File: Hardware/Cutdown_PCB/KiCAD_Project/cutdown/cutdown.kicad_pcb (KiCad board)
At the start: 4 copper layers, 24.1 x 60.3 mm, 26 parts, among them J1 Nichrome Wire, Q1 MMBT3904, U1 Particle, U2 BMP388, U3 ublox_SAM-M8Q

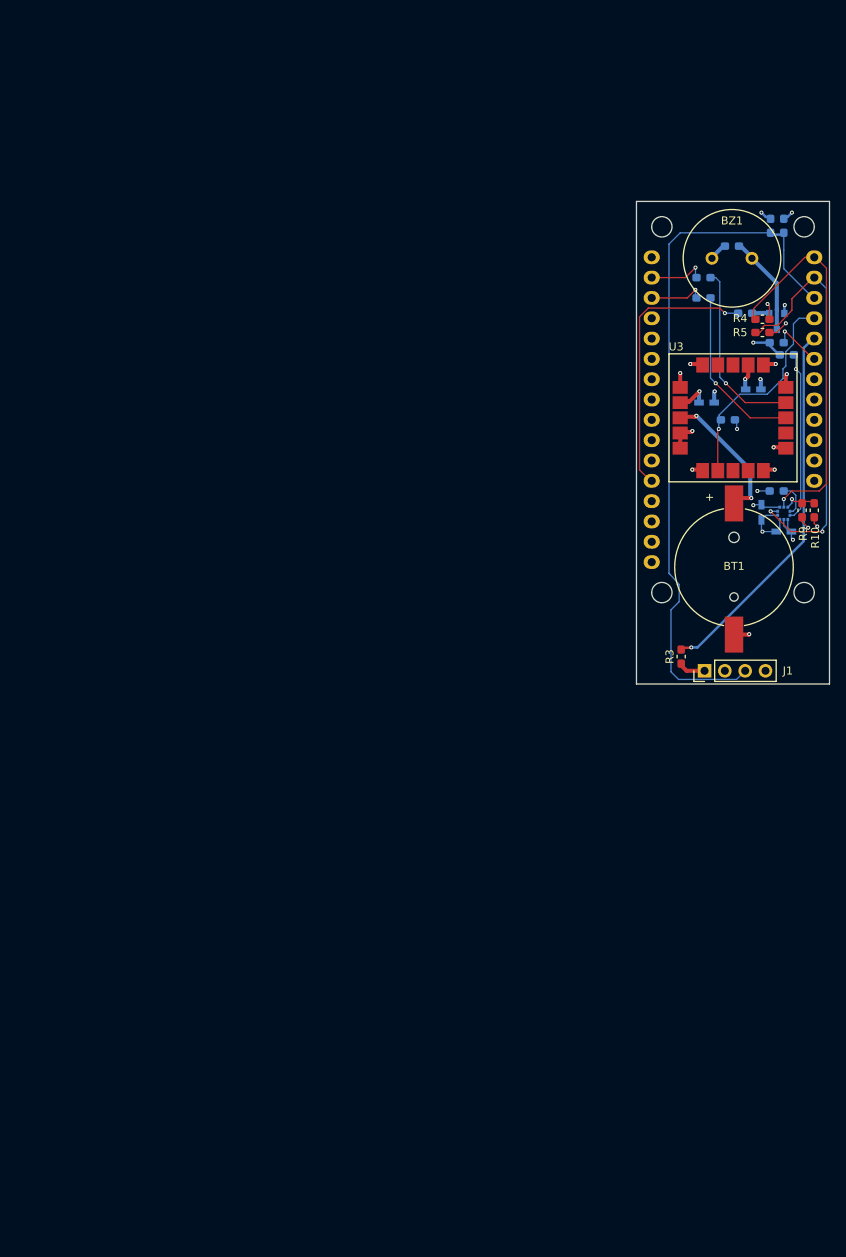
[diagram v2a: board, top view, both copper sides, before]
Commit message: Remove cutdown power pcb and update cutdown design
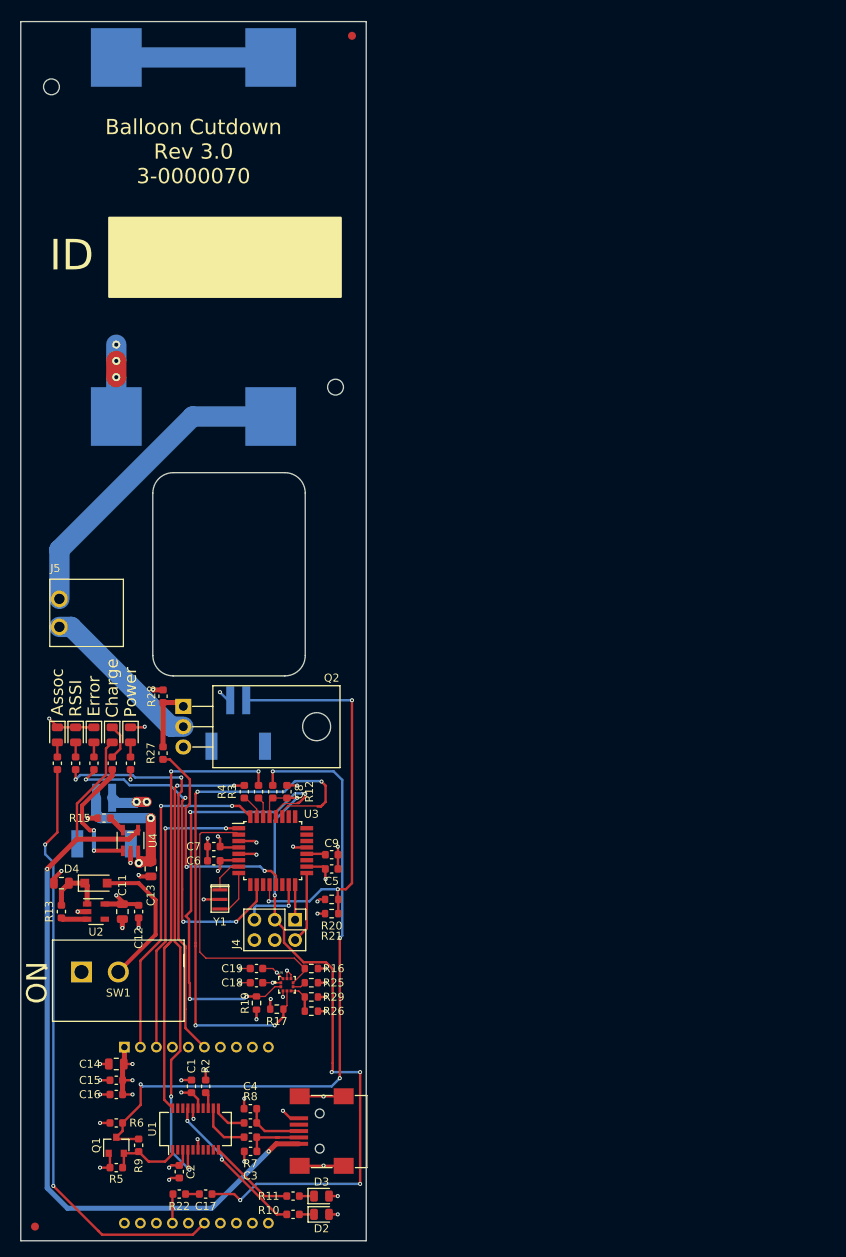
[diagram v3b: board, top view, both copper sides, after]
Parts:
- removed BZ1: Buzzer, lib_fp:PS1240P02BT
- added BT2: CR123, lib_fp:1-0000782, B.Cu at (133.3, 52.1)
- added C10: 1-0000075, capacitors_0805:1-0000075, F.Cu at (107.2, 132.8)
- added C11: 1-0000075, capacitors_0805:1-0000075, F.Cu at (114.8, 136.4)
- added C12: 1-0000018, capacitors_0603:1-0000018, F.Cu at (116.8, 136.4)
- added C13: 1-0000075, capacitors_0805:1-0000075, F.Cu at (118.4, 131.1)
- added C14: 1-0000075, capacitors_0805:1-0000075, F.Cu at (114.0, 155.4)
- added C15: 1-0000018, capacitors_0603:1-0000018, F.Cu at (114.0, 157.5)
- added C16: 1-0000007, capacitors_0603:1-0000007, F.Cu at (114.0, 159.3)
- added C17: 1-0000007, capacitors_0603:1-0000007, F.Cu at (125.2, 171.7)
- added C18: 0.1u, Capacitor_SMD:C_0603_1608Metric, F.Cu at (131.6, 145.3)
- added C19: 0.1u, Capacitor_SMD:C_0603_1608Metric, F.Cu at (131.6, 143.5)
- added C5: 1-0000007, capacitors_0603:1-0000007, F.Cu at (141.0, 131.1)
- added C6: 1-0000007, capacitors_0603:1-0000007, F.Cu at (126.2, 130.0)
- added C7: 1-0000007, capacitors_0603:1-0000007, F.Cu at (126.2, 128.3)
- added C8: 1-0000007, capacitors_0603:1-0000007, F.Cu at (133.6, 121.4)
- added C9: 1-0000007, capacitors_0603:1-0000007, F.Cu at (141.0, 129.3)
- added D1: Green, LED_SMD:LED_0805_2012Metric, F.Cu at (115.8, 114.3)
- added D2: Yellow, LED_SMD:LED_0805_2012Metric, F.Cu at (139.7, 174.2)
- added D3: Red, LED_SMD:LED_0805_2012Metric, F.Cu at (139.7, 172.0)
- added D4: D_Schottky, Diode_SMD:D_SOD-123F, F.Cu at (111.5, 132.8)
- added D5: Yellow, LED_SMD:LED_0805_2012Metric, F.Cu at (113.5, 114.3)
- added D6: Red, LED_SMD:LED_0805_2012Metric, F.Cu at (111.3, 114.3)
- added D7: Blue, LED_SMD:LED_0805_2012Metric, F.Cu at (109.0, 114.3)
- added D8: Yellow, LED_SMD:LED_0805_2012Metric, F.Cu at (106.7, 114.3)
- added FID1: Fiducial, Fiducial:Fiducial_1mm_Mask2mm, F.Cu at (143.5, 26.9)
- added FID2: Fiducial, Fiducial:Fiducial_1mm_Mask2mm, F.Cu at (103.9, 175.8)
- added J2: Battery LiPO 1S, lib_fp:JST_S2B-PH-SM4-TB(LF)(SN), B.Cu at (112.5, 122.2)
- added J3: External Cutdown, lib_fp:JST_S2B-PH-SM4-TB(LF)(SN), B.Cu at (129.3, 110.0)
- added J4: ISP, Connector_PinHeader_2.54mm:PinHeader_2x03_P2.54mm_Vertical, F.Cu at (136.4, 137.4)
- added J5: Hot Wire, lib_fp:1-0000783, F.Cu at (106.9, 99.1)
- added PCB1: barepcb, lib_fp:barepcb, F.Cu at (278.6, 161.5)
- added Q2: FQP30N06L, Package_TO_SOT_THT:TO-220-3_Horizontal_TabDown, F.Cu at (122.4, 110.7)
- added R16: 10k, Resistor_SMD:R_0603_1608Metric, F.Cu at (138.4, 143.5)
- added R17: 10k, Resistor_SMD:R_0603_1608Metric, F.Cu at (134.1, 148.6)
- added R18: 1-0000008, resistors_0603:1-0000008, F.Cu at (111.3, 117.9)
- added R19: 10k, Resistor_SMD:R_0603_1608Metric, F.Cu at (131.6, 147.8)
- added R20: 10k, Resistor_SMD:R_0603_1608Metric, F.Cu at (141.0, 134.9)
- added R21: NP, Resistor_SMD:R_0603_1608Metric, F.Cu at (141.0, 136.7)
- added R22: 1-0000006, resistors_0603:1-0000006, F.Cu at (121.9, 171.7)
- added R23: 1-0000008, resistors_0603:1-0000008, F.Cu at (109.0, 117.9)
- added R24: 1-0000008, resistors_0603:1-0000008, F.Cu at (106.7, 117.9)
- added R25: 10k, Resistor_SMD:R_0603_1608Metric, F.Cu at (138.4, 145.3)
- added R26: NP, Resistor_SMD:R_0603_1608Metric, F.Cu at (138.4, 148.8)
- added R27: 1-0000006, resistors_0603:1-0000006, F.Cu at (119.9, 116.6)
- added R28: 1-0000010, resistors_0603:1-0000010, F.Cu at (119.9, 109.5)
- added R29: 10k, Resistor_SMD:R_0603_1608Metric, F.Cu at (138.4, 147.1)
- added SW1: SW_SPST, lib_fp:SW_GF-123-0054, F.Cu at (114.3, 145.0)
- added U4: MCP73831, lib_fp:1-0000793, F.Cu at (115.8, 127.5)
- added U5: XBee, lib_fp:XBee, B.Cu at (115.1, 164.3)
- added U6: BMP388, lib_fp:PQFN50P200X200X80-10N, F.Cu at (135.4, 145.5)
- added Y1: 16MHz, lib_fp:Resonator, F.Cu at (127.0, 134.9)
- BT1: value CR1220 -> CR123; footprint lib_fp:S8411-45R -> lib_fp:1-0000782; moved to B.Cu
- C1, C2: value 0.1u -> 1-0000007; footprint Capacitors_SMD:C_0603_HandSoldering -> capacitors_0603:1-0000007; moved to F.Cu
- C3, C4: value 0.1u -> 1-0000017; footprint Capacitors_SMD:C_0603_HandSoldering -> capacitors_0603:1-0000017; moved to F.Cu
- J1: value Nichrome Wire -> Mini_USB_B; footprint Pin_Headers:Pin_Header_Straight_1x04_Pitch2.54mm -> lib_fp:MiniUSB
- Q1: value MMBT3904 -> 2N7002; footprint TO_SOT_Packages_SMD:SOT-23 -> Package_TO_SOT_SMD:SOT-23; moved to F.Cu
- R1: value 10k -> 1-0000008; footprint Resistor_SMD:R_0603_1608Metric_Pad1.05x0.95mm_HandSolder -> resistors_0603:1-0000008; moved to F.Cu
- R10: value 10k -> 1-0000008; footprint Resistor_SMD:R_0603_1608Metric_Pad1.05x0.95mm_HandSolder -> resistors_0603:1-0000008
- R11: value 1k -> 1-0000008; footprint Resistor_SMD:R_0603_1608Metric_Pad1.05x0.95mm_HandSolder -> resistors_0603:1-0000008; moved to F.Cu
- R12: value 1k -> 1-0000010; footprint Resistor_SMD:R_0603_1608Metric_Pad1.05x0.95mm_HandSolder -> resistors_0603:1-0000010; moved to F.Cu
- R13: value 10k -> 1-0000174; footprint Resistor_SMD:R_0603_1608Metric_Pad1.05x0.95mm_HandSolder -> resistors_0603:1-0000174; moved to F.Cu
- R14: value 0R0 -> 1-0000013; footprint Resistor_SMD:R_0603_1608Metric_Pad1.05x0.95mm_HandSolder -> resistors_0603:1-0000013; moved to F.Cu
- R15: value 0R0 -> 1-0000010; footprint Resistor_SMD:R_0603_1608Metric_Pad1.05x0.95mm_HandSolder -> resistors_0603:1-0000010; moved to F.Cu
- R2: value 10k -> 1-0000006; footprint Resistor_SMD:R_0603_1608Metric_Pad1.05x0.95mm_HandSolder -> resistors_0603:1-0000006; moved to F.Cu
- R3: value 0R0 -> 1-0000013; footprint Resistor_SMD:R_0603_1608Metric_Pad1.05x0.95mm_HandSolder -> resistors_0603:1-0000013
- R4: value 10k -> 1-0000013; footprint Resistor_SMD:R_0603_1608Metric_Pad1.05x0.95mm_HandSolder -> resistors_0603:1-0000013
- R5: value 10k -> 1-0000010; footprint Resistor_SMD:R_0603_1608Metric_Pad1.05x0.95mm_HandSolder -> resistors_0603:1-0000010
- R6: value 10k -> 1-0000010; footprint Resistor_SMD:R_0603_1608Metric_Pad1.05x0.95mm_HandSolder -> resistors_0603:1-0000010; moved to F.Cu
- R7: value 10k -> 1-0000012; footprint Resistor_SMD:R_0603_1608Metric_Pad1.05x0.95mm_HandSolder -> resistors_0603:1-0000012; moved to F.Cu
- R8: value NP -> 1-0000012; footprint Resistor_SMD:R_0603_1608Metric_Pad1.05x0.95mm_HandSolder -> resistors_0603:1-0000012; moved to F.Cu
- R9: value NP -> 1-0000006; footprint Resistor_SMD:R_0603_1608Metric_Pad1.05x0.95mm_HandSolder -> resistors_0603:1-0000006
- U1: value Particle -> FT231XS; footprint lib_fp:Particle -> Package_SO:SSOP-20_3.9x8.7mm_P0.635mm; moved to F.Cu
- U2: value BMP388 -> SPX3819M5-L-3-3; footprint lib_fp:PQFN50P200X200X80-10N -> Package_TO_SOT_SMD:SOT-23-5; moved to F.Cu
- U3: value ublox_SAM-M8Q -> ATmega328P-AU; footprint lib_fp:SAM-M8Q -> Package_QFP:TQFP-32_7x7mm_P0.8mm
- moved R7 132.0 mm to (130.8, 164.6), turned to 0 degrees
- moved R5 132.0 mm to (114.0, 168.4)
- moved Q1 132.0 mm to (114.0, 165.6), turned to 90 degrees
- moved R8 129.6 mm to (130.8, 162.8), turned to 0 degrees
- moved R11 124.0 mm to (136.1, 172.0)
- moved R2 116.8 mm to (125.2, 158.2), turned to 90 degrees
- moved R6 116.5 mm to (114.0, 162.8)
- moved R9 114.8 mm to (116.8, 165.6)
- moved C3 114.1 mm to (130.8, 166.4)
- moved U1 112.2 mm to (124.0, 163.6)
- moved C2 110.1 mm to (121.9, 168.9), turned to 270 degrees
- moved R10 109.5 mm to (136.1, 174.2), turned to 180 degrees
- moved C4 105.1 mm to (130.8, 161.0)
- moved R13 103.7 mm to (107.2, 136.4), turned to 270 degrees
- moved C1 101.1 mm to (123.4, 158.2)
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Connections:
- BT1 pad 1: +BATT -> Net-(BT1-Pad1)
- C2 pad 1: GND -> +3V3
- C2 pad 2: +3V3 -> GND
- C3 pad 1: GND -> Net-(C3-Pad1)
- C3 pad 2: +3V3 -> GND
- C4 pad 1: GND -> Net-(C4-Pad1)
- C4 pad 2: +3V3 -> GND
- J1 pad 1: Net-(J1-Pad1) -> +5V
- J1 pad 2: GND -> Net-(C3-Pad1)
- J1 pad 3: EXT_CUTDOWN -> Net-(C4-Pad1)
- J1 pad 4: GND -> (no net)
- Q1 pad 1: Net-(Q1-Pad1) -> +3V3
- Q1 pad 2: GND -> Net-(Q1-Pad2)
- Q1 pad 3: Net-(BZ1-Pad2) -> DTR
- R1 pad 1: +3V3 -> Net-(D1-Pad2)
- R1 pad 2: BMP388_SDO -> +3V3
- R10 pad 1: Net-(R10-Pad1) -> Net-(D2-Pad1)
- R10 pad 2: GND -> Net-(R10-Pad2)
- R11 pad 1: Net-(Q1-Pad1) -> Net-(D3-Pad1)
- R11 pad 2: PIEZO_ELEMENT -> Net-(R11-Pad2)
- R12 pad 2: Net-(BZ1-Pad2) -> RESET
- R13 pad 1: +3V3 -> Net-(C10-Pad1)
- R14 pad 2: GPS_TX -> Net-(D5-Pad1)
- R15 pad 2: GPS_RX -> GND
- R2 pad 1: +3V3 -> Net-(R2-Pad1)
- R2 pad 2: BMP388_INT -> +3V3
- R3 pad 1: Net-(J1-Pad1) -> RXI
- R3 pad 2: CUTOFF_LOGIC -> Net-(R3-Pad2)
- R4 pad 1: +3V3 -> TXO
- R4 pad 2: SDA -> Net-(R4-Pad2)
- R5 pad 1: +3V3 -> Net-(Q1-Pad2)
- R5 pad 2: SCL -> +3V3
- R6 pad 1: +3V3 -> DTR
- R6 pad 2: GPS_PPS -> +3V3
- R7 pad 1: +3V3 -> Net-(R7-Pad1)
- R7 pad 2: EXT_CUTDOWN -> Net-(C3-Pad1)
- R8 pad 1: GND -> Net-(R8-Pad1)
- R8 pad 2: EXT_CUTDOWN -> Net-(C4-Pad1)
- R9 pad 1: +3V3 -> Net-(Q1-Pad2)
- R9 pad 2: Net-(R10-Pad1) -> DTR
- U1 pad 1: Net-(U1-Pad1) -> Net-(Q1-Pad2)
- U1 pad 10: Net-(U1-Pad10) -> Net-(R11-Pad2)
- U1 pad 11: Net-(U1-Pad11) -> Net-(R8-Pad1)
- U1 pad 12: Net-(U1-Pad12) -> Net-(R7-Pad1)
- U1 pad 13: Net-(U1-Pad13) -> Net-(R2-Pad1)
- U1 pad 14: Net-(R14-Pad1) -> (no net)
- U1 pad 15: Net-(R15-Pad1) -> +3V3
- U1 pad 16: Net-(U1-Pad16) -> GND
- U1 pad 17: Net-(U1-Pad17) -> Net-(R10-Pad2)
- U1 pad 18: Net-(U1-Pad18) -> (no net)
- U1 pad 19: Net-(U1-Pad19) -> (no net)
- U1 pad 2: +3V3 -> (no net)
- U1 pad 20: Net-(U1-Pad20) -> Net-(R3-Pad2)
- U1 pad 3: Net-(U1-Pad3) -> +3V3
- U1 pad 4: GND -> Net-(R4-Pad2)
- U1 pad 5: PIEZO_ELEMENT -> (no net)
- U1 pad 6: Net-(U1-Pad6) -> GND
- U1 pad 7: Net-(U1-Pad7) -> (no net)
- U1 pad 8: Net-(U1-Pad8) -> (no net)
- U1 pad 9: Net-(U1-Pad9) -> (no net)
- U2 pad 1: +3V3 -> Net-(C10-Pad1)
- U2 pad 2: SCL -> GND
- U2 pad 3: GND -> Net-(R13-Pad2)
- U2 pad 4: SDA -> (no net)
- U2 pad 5: Net-(R10-Pad1) -> +3V3
- U3 pad 1: GND -> XBee_from_uC
- U3 pad 10: GND -> Net-(R18-Pad2)
- U3 pad 11: GND -> (no net)
- U3 pad 12: Net-(U3-Pad12) -> EXT_CUTDOWN
- U3 pad 13: GPS_TX -> Cutdown_Command
- U3 pad 14: GPS_RX -> (no net)
- U3 pad 15: GND -> MOSI
- U3 pad 16: GND -> MISO
- U3 pad 17: +3V3 -> SCK
- U3 pad 18: Net-(U3-Pad18) -> +3V3
- U3 pad 19: Net-(U3-Pad19) -> (no net)
- U3 pad 2: +3V3 -> BMP388_INT
- U3 pad 20: GND -> Net-(C9-Pad1)
- U3 pad 3: +BATT -> GND
- U3 pad 4: GND -> +3V3
- U3 pad 6: GND -> +3V3
- U3 pad 7: GPS_PPS -> Net-(U3-Pad7)
- U3 pad 9: Net-(U3-Pad9) -> (no net)
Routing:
- net +5V: track 0.00 -> 103.0 mm, vias 0 -> 2
- net DTR: track 0.00 -> 84.5 mm, vias 0 -> 4
- net RESET: track 0.00 -> 82.9 mm, vias 0 -> 6
- net Net-(R24-Pad2): track 0.00 -> 75.1 mm, vias 0 -> 2
- net Net-(R4-Pad2): track 0.00 -> 60.8 mm, vias 0 -> 4
- net Net-(R3-Pad2): track 0.00 -> 56.4 mm, vias 0 -> 2
- net GND: track 30.3 -> 80.7 mm, vias 16 -> 40
- net Net-(R23-Pad1): track 0.00 -> 50.0 mm, vias 0 -> 2
- net CUTOFF_LOGIC: track 46.8 -> 0.00 mm, vias 1 -> 0
- net Net-(R18-Pad2): track 0.00 -> 43.6 mm, vias 0 -> 4
- net XBee_to_uC: track 0.00 -> 42.9 mm, vias 0 -> 2
- net Net-(BT2-Pad1): track 0.00 -> 39.5 mm
- net XBee_from_uC: track 0.00 -> 37.0 mm, vias 0 -> 2
- net EXT_CUTDOWN: track 89.0 -> 52.6 mm, vias 0 -> 3
- net PIEZO_ELEMENT: track 34.0 -> 0.00 mm, vias 1 -> 0
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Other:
- board size 24.1 x 60.3 mm -> 43.2 x 152.4 mm
- board text added: "Assoc"
- board text added: "BATT"
- board text added: "Balloon Cutdown Rev 3.0 3-0000070"
- board text added: "Charge"
- board text added: "EXT"
- board text added: "Error"
- board text added: "ID"
- board text added: "ON"
- board text added: "Power"
- board text added: "RSSI"
- board text removed: "Balloon Cutdown Module Rev. 2.0 April 2020 P/N 3-0000028"
- board text removed: "Cut"
- board text removed: "Ext"

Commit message: Tweaks
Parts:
- moved J5 5.07 mm to (105.0, 94.4)
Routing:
- net Net-(J5-Pad2): track 20.7 -> 32.3 mm
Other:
- outline, holes or cut-outs redrawn
- board text added: "Chg"
- board text added: "Err"
- board text added: "Pwr"
- board text removed: "Charge"
- board text removed: "Error"
- board text removed: "Power"

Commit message: Update production files
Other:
- rule pad_to_mask_clearance: 0.0508 -> 0

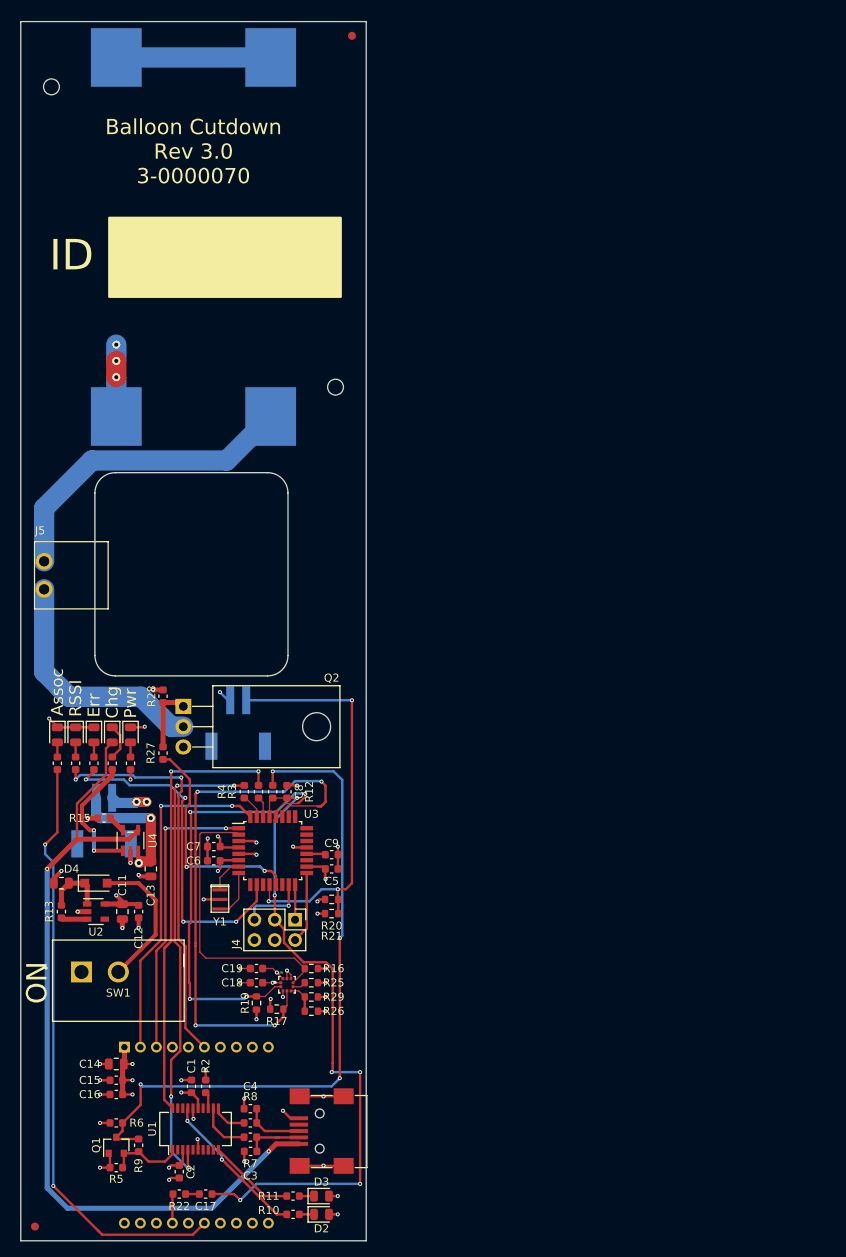
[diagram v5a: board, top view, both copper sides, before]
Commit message: Move batteries, remove charging circuit, add mounting holes.
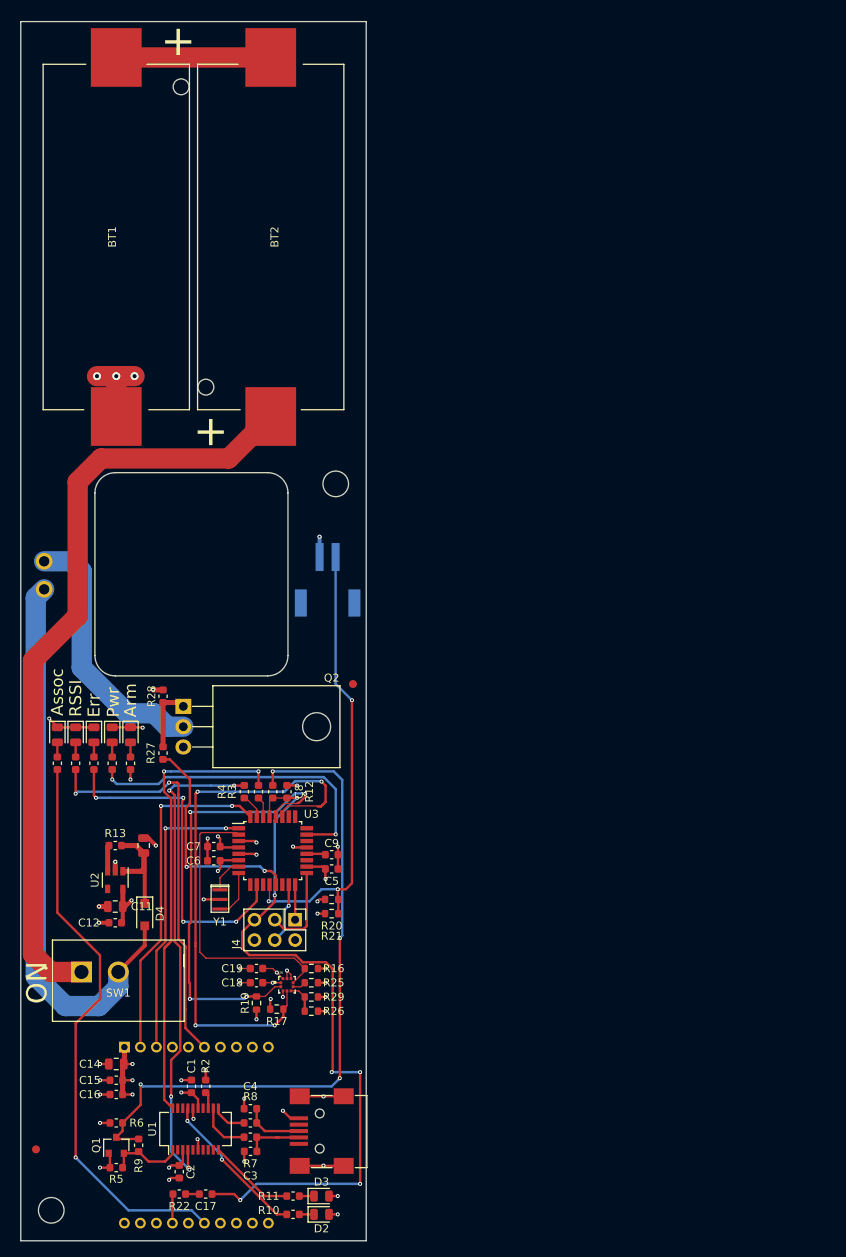
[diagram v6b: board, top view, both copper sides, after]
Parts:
- removed C13: 1-0000075, capacitors_0805:1-0000075
- removed J2: Battery LiPO 1S, lib_fp:JST_S2B-PH-SM4-TB(LF)(SN)
- removed R15: 1-0000010, resistors_0603:1-0000010
- removed U4: MCP73831, lib_fp:1-0000793
- added H1: M3_ISO_7380, mechanical:MountingHole_3.2mm_M3_ISO7380, F.Cu at (105.9, 173.7)
- added H2: M3_ISO_7380, mechanical:MountingHole_3.2mm_M3_ISO7380, F.Cu at (141.5, 82.9)
- BT1, BT2: moved to F.Cu
- D5: value Yellow -> 1-0000601; footprint LED_SMD:LED_0805_2012Metric -> leds_0805:1-0000601
- J5: moved to B.Cu
- R14: value 1-0000013 -> 1-0000008; footprint resistors_0603:1-0000013 -> resistors_0603:1-0000008
- Y1: value 16MHz -> 8MHz
- moved FID1 81.0 mm to (143.6, 108.0)
- moved J3 21.1 mm to (140.5, 92.1)
- moved C10 11.3 mm to (117.5, 128.1), turned to 90 degrees
- moved R13 10.7 mm to (113.9, 128.1), turned to 180 degrees
- moved FID2 9.65 mm to (104.0, 166.1)
- moved D4 7.26 mm to (117.6, 136.8), turned to 270 degrees
- moved U2 4.62 mm to (113.9, 132.5), turned to 270 degrees
- moved C12 3.24 mm to (113.9, 137.8), turned to 180 degrees
- moved C11 1.09 mm to (113.9, 135.8), turned to 180 degrees
- turned J5 to 90 degrees
- turned R14 to 270 degrees
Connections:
- C10 pad 1: Net-(C10-Pad1) -> +BATT
- D4 pad 1: Net-(C10-Pad1) -> +BATT
- D4 pad 2: Net-(D4-Pad2) -> SW_PWR
- D5 pad 1: Net-(D5-Pad1) -> GND
- D5 pad 2: +5V -> Net-(D5-Pad2)
- J1 pad 1: +5V -> (no net)
- J4 pad 2: SCK -> +3V3
- J4 pad 3: RESET -> SCK
- J4 pad 4: GND -> MOSI
- J4 pad 5: MOSI -> RESET
- J4 pad 6: +3V3 -> GND
- J5 pad 1: Net-(BT2-Pad1) -> SW_PWR
- R13 pad 1: Net-(C10-Pad1) -> +BATT
- R14 pad 1: Net-(R14-Pad1) -> Net-(D5-Pad2)
- R14 pad 2: Net-(D5-Pad1) -> Net-(R14-Pad2)
- SW1 pad 1: +BATT -> Net-(BT2-Pad1)
- SW1 pad 2: Net-(D4-Pad2) -> SW_PWR
- U2 pad 1: Net-(C10-Pad1) -> +BATT
- U3 pad 23: (no net) -> Net-(R14-Pad2)
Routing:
- net +5V: track 103.0 -> 0.00 mm, vias 2 -> 0
- net SW_PWR: track 0.00 -> 70.7 mm
- net Net-(BT2-Pad1): track 39.7 -> 103.0 mm
- net Net-(R14-Pad2): track 0.00 -> 39.7 mm, vias 0 -> 2
- net +BATT: track 35.6 -> 14.2 mm, vias 2 -> 0
- net Net-(D4-Pad2): track 17.9 -> 0.00 mm
- net Net-(R14-Pad1): track 16.2 -> 0.00 mm, vias 2 -> 0
- net Net-(C10-Pad1): track 7.87 -> 0.00 mm
- net RESET: track 82.9 -> 89.9 mm
- net EXT_CUTDOWN: track 52.6 -> 58.2 mm
- net GND: track 80.7 -> 75.3 mm, vias 40 -> 35
- net Net-(D5-Pad1): track 4.54 -> 0.00 mm
- net Net-(R24-Pad2): track 75.1 -> 71.5 mm, vias 2 -> 1
- net SCK: track 8.98 -> 11.3 mm
- net Net-(R15-Pad1): track 2.19 -> 0.00 mm
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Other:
- board text added: "Arm"
- board text added: "Balloon Cutdown Rev 3.1 3-0000XXX"
- board text removed: "Balloon Cutdown Rev 3.0 3-0000070"
- board text removed: "Chg"

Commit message: Reannotate
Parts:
- moved PCB1 138.0 mm to (141.9, 179.8)
- renumbered C14 to C13, C15 to C14, C16 to C15, C17 to C16, C18 to C17, C19 to C18, J3 to J2, J4 to J3, J5 to J4, R16 to R15, R17 to R16, R18 to R17, R19 to R18, R20 to R19, R21 to R20, R22 to R21, R23 to R22, R24 to R23, R25 to R24, R26 to R25, R27 to R26, R28 to R27, R29 to R28, U5 to U4, U6 to U5
